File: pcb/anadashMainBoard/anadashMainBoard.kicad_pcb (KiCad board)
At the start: 2 copper layers, 100 x 50 mm, 17 parts, among them J1 DisplayConnector, J2 LeftKeyConnector, J3 RightKeyConnector, J4 EncoderConnector

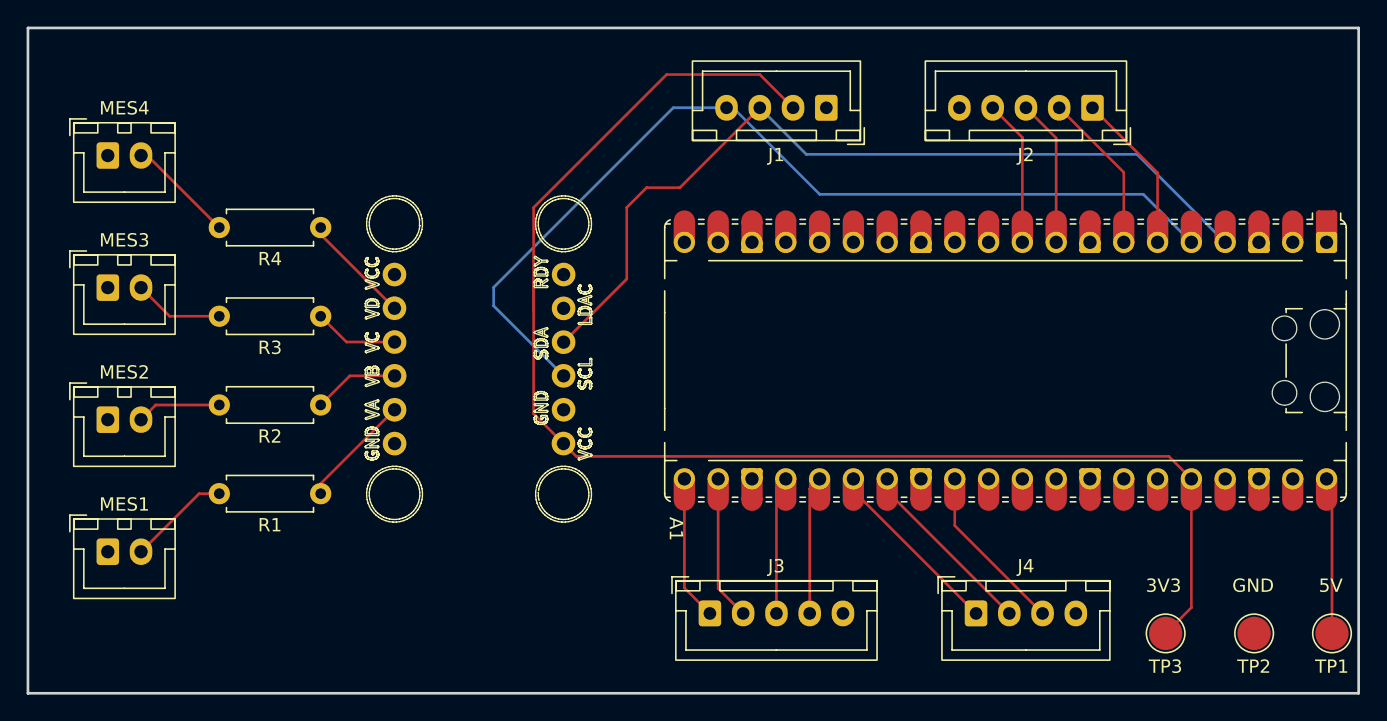
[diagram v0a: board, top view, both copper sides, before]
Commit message: Finish the mainboard PCB
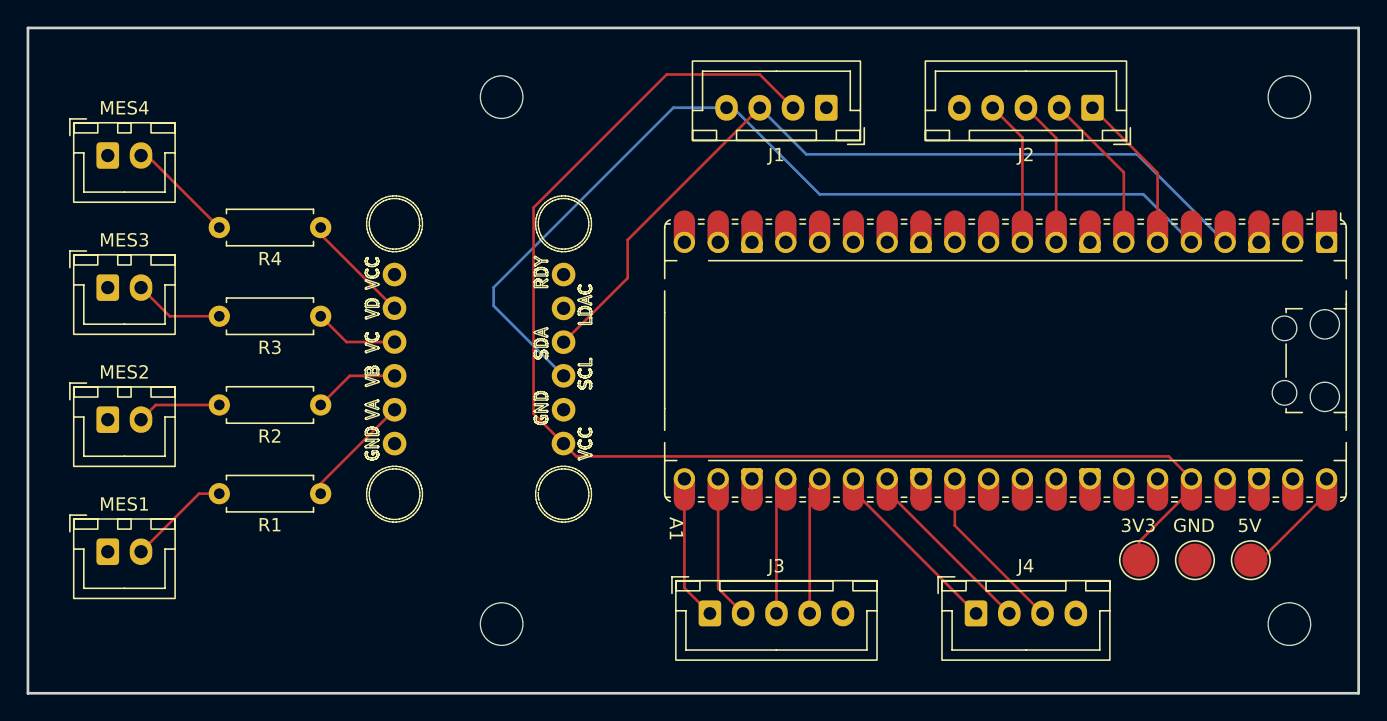
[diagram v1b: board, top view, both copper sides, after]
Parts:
- added REF**: MountingHole_3.2mm_M3, MountingHole:MountingHole_3.2mm_M3, F.Cu at (202.8, 114.8)
- added REF**: MountingHole_3.2mm_M3, MountingHole:MountingHole_3.2mm_M3, F.Cu at (143.6, 114.8)
- added REF**: MountingHole_3.2mm_M3, MountingHole:MountingHole_3.2mm_M3, F.Cu at (143.6, 75.2)
- added REF**: MountingHole_3.2mm_M3, MountingHole:MountingHole_3.2mm_M3, F.Cu at (202.8, 75.2)
- moved TP1 8.21 mm to (199.9, 110.0)
- moved TP2 7.07 mm to (195.7, 110.0)
- moved TP3 5.85 mm to (191.5, 110.0)
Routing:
- net +3V3: track 104.4 -> 99.0 mm
- net SDA: track 66.7 -> 62.9 mm
- net +5V: track 11.8 -> 9.61 mm

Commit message: Fixing alignment, improvements to pcb such as silkscreen.
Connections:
- U1 pad 1: unconnected-(U1-GND-Pad1) -> GND
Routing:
- net SCL: track 71.0 -> 70.5 mm
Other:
- board text added: "DisplayConnector"
- board text added: "EncoderConnector"
- board text added: "LeftKeyConnector"
- board text added: "RightKeyConnector"
- board text added: "When connecting,make sure GND is aligned! On this board, GND is always the rightmost pin."
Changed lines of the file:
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@@
 	)
 	(footprint "Adafruit_MCP4728:Adafruit_MCP4728"
-		(locked yes)
 		(layer "F.Cu")
 		(at 150.813699 107.646126 90)
@@
 			(layers "*.Cu" "*.Mask")
 			(remove_unused_layers no)
-			(net "unconnected-(U1-GND-Pad1)")
+			(net "GND")
 			(pinfunction "GND_1")
-			(pintype "power_in+no_connect")
+			(pintype "power_in")
 			(solder_mask_margin 0.0508)
 			(thermal_bridge_angle 0)
@@
 			)
 		)
-		(pad "1" thru_hole roundrect
+		(pad "1" thru_hole oval
 			(at 0 0 180)
 			(size 1.7 1.95)
@@
 			(layers "*.Cu" "*.Mask")
 			(remove_unused_layers no)
-			(roundrect_rratio 0.147059)
 			(net "Net-(A1-GPIO4)")
 			(pinfunction "Pin_1_1")
@@
 			(pintype "passive")
 		)
-		(pad "5" thru_hole oval
+		(pad "5" thru_hole roundrect
 			(at 10 0 180)
 			(size 1.7 1.95)
@@
 			(layers "*.Cu" "*.Mask")
 			(remove_unused_layers no)
+			(roundrect_rratio 0.147059)
 			(net "GND")
 			(pinfunction "Pin_5_5")
@@
 			)
 		)
-		(pad "1" thru_hole roundrect
+		(pad "1" thru_hole oval
 			(at 0 0)
 			(size 1.7 1.95)
@@
 			(layers "*.Cu" "*.Mask")
 			(remove_unused_layers no)
-			(roundrect_rratio 0.147059)
 			(net "Net-(A1-GPIO20)")
 			(pinfunction "Pin_1_1")
@@
 			(pintype "passive")
 		)
-		(pad "4" thru_hole oval
+		(pad "4" thru_hole roundrect
 			(at 7.5 0)
 			(size 1.7 1.95)
@@
 			(layers "*.Cu" "*.Mask")
 			(remove_unused_layers no)
+			(roundrect_rratio 0.147059)
 			(net "GND")
 			(pinfunction "Pin_4_4")
@@
 		(layer "Edge.Cuts")
 	)
+	(gr_text "When connecting,make sure GND is aligned! \nOn this board, GND is always the rightmost pin."
+		(at 119.7 110.9 0)
+		(layer "F.SilkS")
+		(effects
+			(font
+				(size 1 1)
+				(thickness 0.15)
+			)
+			(justify left bottom)
+		)
+	)
+	(gr_text "DisplayConnector\n"
+		(at 157.672618 81.7 0)
+		(layer "F.SilkS")
+		(effects
+			(font
+				(size 1 1)
+				(thickness 0.15)
+			)
+			(justify left bottom)
+		)
+	)
+	(gr_text "LeftKeyConnector\n"
+		(at 176.398808 81.7 0)
+		(layer "F.SilkS")
+		(effects
+			(font
+				(size 1 1)
+				(thickness 0.15)
+			)
+			(justify left bottom)
+		)
+	)
 	(gr_text "3V3\n"
 		(at 190.1 108 0)
@@
 		)
 	)
+	(gr_text "RightKeyConnector"
+		(at 164.25 118.6 0)
+		(layer "F.SilkS")
+		(effects
+			(font
+				(size 1 1)
+				(thickness 0.15)
+			)
+		)
+	)
+	(gr_text "EncoderConnector"
+		(at 183 118.5 0)
+		(layer "F.SilkS")
+		(effects
+			(font
+				(size 1 1)
+				(thickness 0.15)
+			)
+		)
+	)
 	(segment
 		(start 195.4325 104.69)
@@
 		(width 0.2)
 		(layer "B.Cu")
-		(net "SCL")
-	)
-	(segment
-		(start 161 76)
-		(end 160.5 76)
-		(width 0.2)
-		(layer "B.Cu")

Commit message: change to thermal relief pads
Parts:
- moved J4 0.11 mm to (179.2, 113.9)
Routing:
- net +3V3: track 99.0 -> 90.3 mm, vias 0 -> 1

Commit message: added 3d files, or so I hopew
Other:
- board size 100 x 50 mm -> 99.9 x 49.9 mm
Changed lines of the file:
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@@
 		(capping no)
 		(filling no)
+		(grid_origin 108 120)
 		(pcbplotparams
 			(layerselection 0x00000000_00000000_55555555_5755f5ff)
@@
 	)
 	(gr_rect
-		(start 108 70)
-		(end 208 120)
+		(start 108.1 70)
+		(end 208 119.9)
 		(stroke
 			(width 0.2)
@@
 	)
 	(segment
-		(start 153.07 88.798825)
-		(end 153.07 85.93)
+		(start 131.938459 93.605126)
+		(end 130 91.666667)
 		(width 0.2)
 		(layer "F.Cu")
-		(net "SDA")
+		(net "Net-(U1-VC)")
 	)
 	(segment
-		(start 153.07 85.93)
-		(end 163 76)
+		(start 135.555699 93.605126)
+		(end 131.938459 93.605126)
 		(width 0.2)
 		(layer "F.Cu")
-		(net "SDA")
+		(net "Net-(U1-VC)")
 	)
 	(segment
-		(start 148.255699 93.613126)
-		(end 153.07 88.798825)
+		(start 135.546699 91.065126)
+		(end 130 85.518427)
 		(width 0.2)
 		(layer "F.Cu")
-		(net "SDA")
-	)
-	(segment
-		(start 166.5 79.5)
-		(end 191.3625 79.5)
-		(width 0.2)
-		(layer "B.Cu")
-		(net "SDA")
-	)
-	(segment
-		(start 163 76)
-		(end 166.5 79.5)
-		(width 0.2)
-		(layer "B.Cu")
-		(net "SDA")
+		(net "Net-(U1-VD)")
 	)
 	(segment
-		(start 191.3625 79.5)
-		(end 197.9725 86.11)
+		(start 130 85.518427)
+		(end 130 85)
 		(width 0.2)
-		(layer "B.Cu")
-		(net "SDA")
+		(layer "F.Cu")
+		(net "Net-(U1-VD)")
 	)
 	(segment
@@
 	)
 	(segment
+		(start 153.07 88.798825)
+		(end 153.07 85.93)
+		(width 0.2)
+		(layer "F.Cu")
+		(net "SDA")
+	)
+	(segment
+		(start 153.07 85.93)
+		(end 163 76)
+		(width 0.2)
+		(layer "F.Cu")
+		(net "SDA")
+	)
+	(segment
+		(start 148.255699 93.613126)
+		(end 153.07 88.798825)
+		(width 0.2)
+		(layer "F.Cu")
+		(net "SDA")
+	)
+	(segment
+		(start 166.5 79.5)
+		(end 191.3625 79.5)
+		(width 0.2)
+		(layer "B.Cu")
+		(net "SDA")
+	)
+	(segment
+		(start 163 76)
+		(end 166.5 79.5)
+		(width 0.2)
+		(layer "B.Cu")
+		(net "SDA")
+	)
+	(segment
+		(start 191.3625 79.5)
+		(end 197.9725 86.11)
+		(width 0.2)
+		(layer "B.Cu")
+		(net "SDA")
+	)
+	(segment
 		(start 192.8925 80.8925)
 		(end 192.8925 86.11)
@@
 	)
 	(segment
-		(start 131.938459 93.605126)
-		(end 130 91.666667)
-		(width 0.2)
-		(layer "F.Cu")
-		(net "Net-(U1-VC)")
-	)
-	(segment
-		(start 135.555699 93.605126)
-		(end 131.938459 93.605126)
-		(width 0.2)
-		(layer "F.Cu")
-		(net "Net-(U1-VC)")
-	)
-	(segment
-		(start 135.546699 91.065126)
-		(end 130 85.518427)
-		(width 0.2)
-		(layer "F.Cu")
-		(net "Net-(U1-VD)")
-	)
-	(segment
-		(start 130 85.518427)
-		(end 130 85)
-		(width 0.2)
-		(layer "F.Cu")
-		(net "Net-(U1-VD)")
-	)
-	(segment
